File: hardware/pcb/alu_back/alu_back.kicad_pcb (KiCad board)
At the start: 2 copper layers, 132.1 x 114.3 mm, 31 parts, among them J1 SYNC, J2 BUS, J3 FLAGS, J4 OUT, J5 FCTL, J6 LOAD, J7 ARGS, J8 POWER, U1 Register A, U10 74HC125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

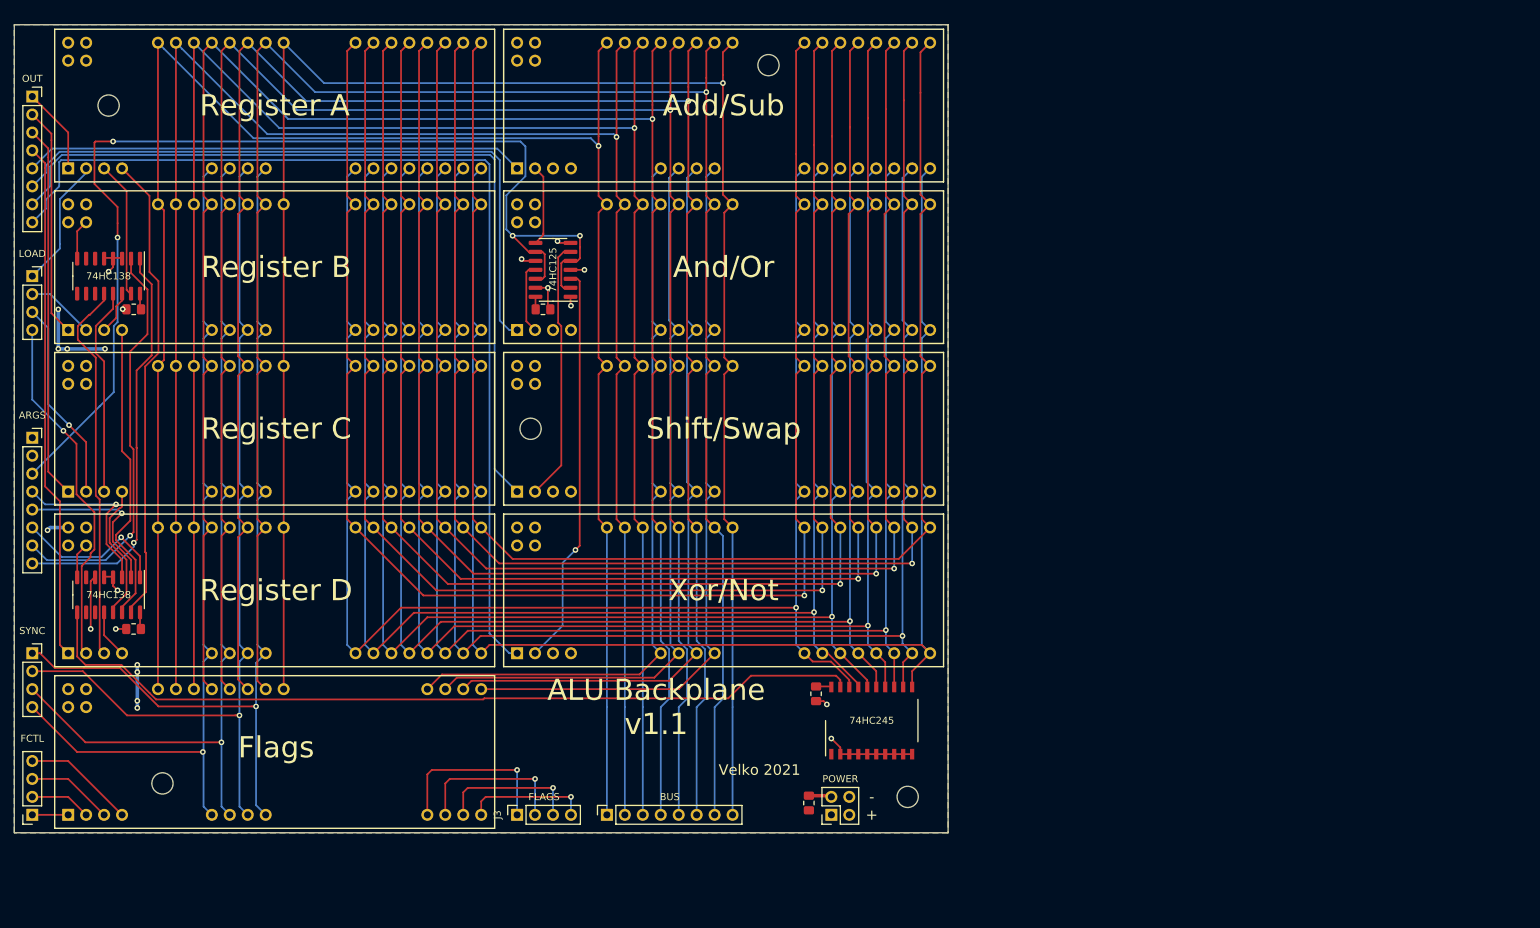
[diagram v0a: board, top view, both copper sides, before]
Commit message: Rewired with internal demuxes, cleaned board
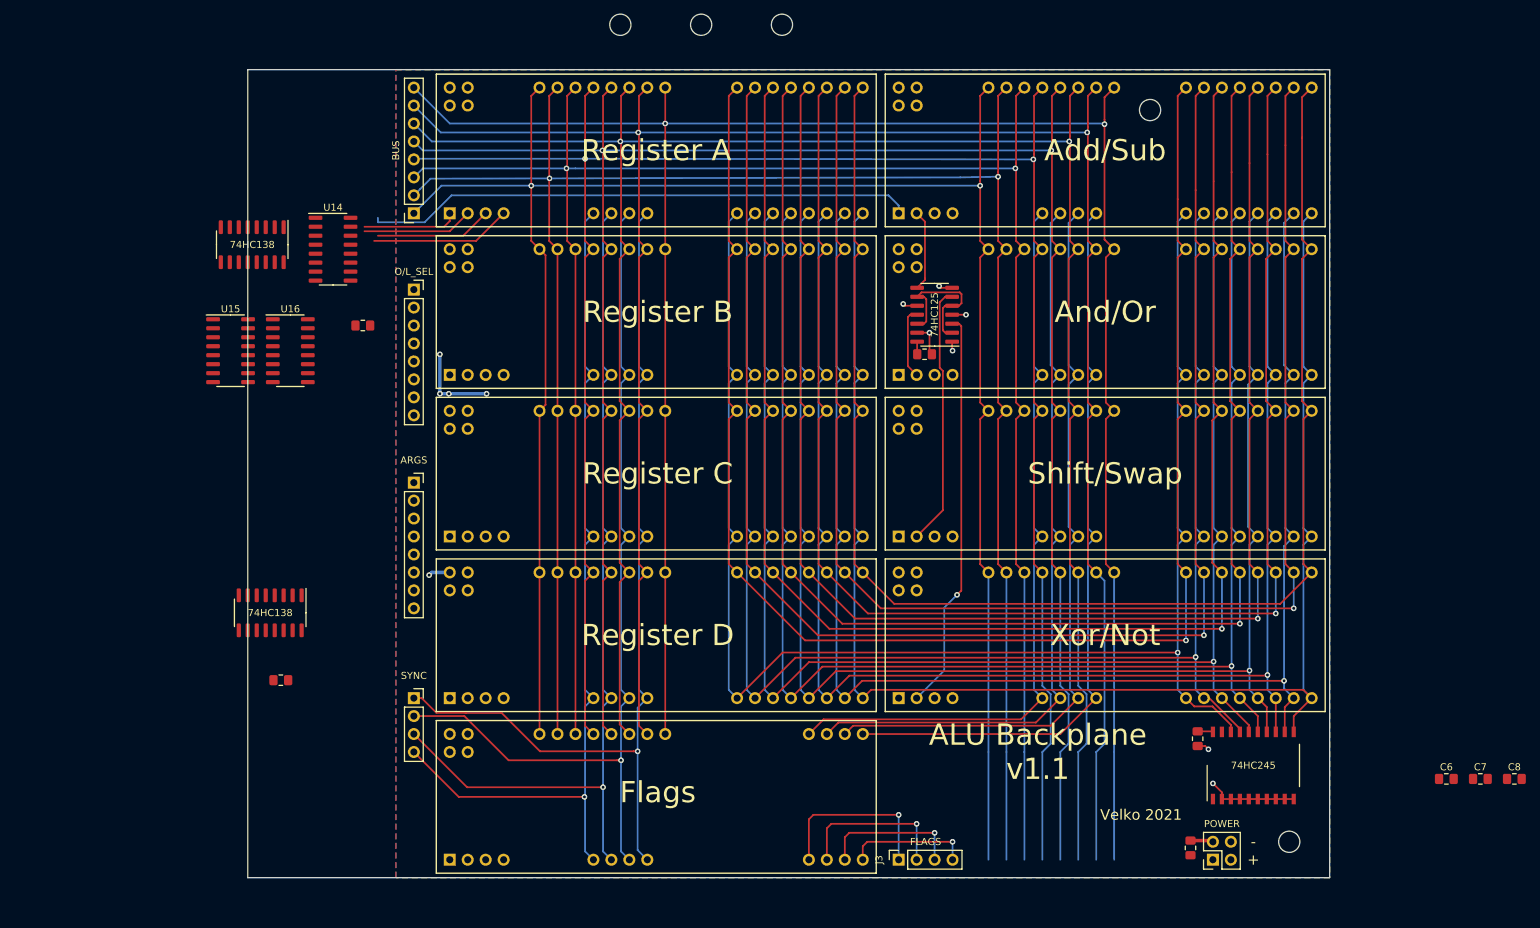
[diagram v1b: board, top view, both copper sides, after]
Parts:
- removed J5: FCTL, Connector_PinSocket_2.54mm:PinSocket_1x04_P2.54mm_Vertical
- removed J6: LOAD, Connector_PinSocket_2.54mm:PinSocket_1x04_P2.54mm_Vertical
- added C6: 100nF, Capacitor_SMD:C_0805_2012Metric_Pad1.18x1.45mm_HandSolder, F.Cu at (224.8, 131.4)
- added C7: 100nF, Capacitor_SMD:C_0805_2012Metric_Pad1.18x1.45mm_HandSolder, F.Cu at (229.6, 131.4)
- added C8: 100nF, Capacitor_SMD:C_0805_2012Metric_Pad1.18x1.45mm_HandSolder, F.Cu at (234.4, 131.4)
- added U14: 74HC138, Package_SO:SOIC-16_3.9x9.9mm_P1.27mm, F.Cu at (67.3, 56.5)
- added U15: 74HC138, Package_SO:SOIC-16_3.9x9.9mm_P1.27mm, F.Cu at (52.8, 70.9)
- added U16: 74HC138, Package_SO:SOIC-16_3.9x9.9mm_P1.27mm, F.Cu at (61.3, 70.9)
- J4: value OUT -> O/L_SEL
- moved H2 138.5 mm to (130.8, 24.8)
- moved J2 89.4 mm to (78.7, 51.4), turned to 180 degrees
- moved H1 73.3 mm to (108.0, 24.8)
- moved H5 62.0 mm to (119.4, 24.8)
- moved J4 60.5 mm to (78.7, 62.2)
- moved J8 54.3 mm to (191.8, 142.9)
- moved U11 54.3 mm to (197.5, 129.5)
- moved C4 54.3 mm to (151.0, 71.4)
- moved U1 54.3 mm to (81.9, 31.8)
- moved U10 54.3 mm to (152.4, 65.8)
- moved U2 54.3 mm to (81.9, 54.6)
- moved U3 54.3 mm to (81.9, 77.5)
- moved U4 54.3 mm to (81.9, 100.3)
- moved U9 54.3 mm to (81.9, 123.2)
- moved C1 54.3 mm to (188.6, 141.2)
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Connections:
- J4 pad 1: OUT_A -> OUT_SEL0
- J4 pad 2: OUT_B -> OUT_SEL1
- J4 pad 3: OUT_C -> OUT_SEL2
- J4 pad 4: OUT_D -> OUT_SEL3
- J4 pad 5: OUT_AS -> LOAD_SEL0
- J4 pad 6: OUT_AO -> LOAD_SEL1
- J4 pad 7: OUT_S -> LOAD_SEL2
- J4 pad 8: OUT_XN -> LOAD_SEL3
- J7 pad 1: (no net) -> CARRY
- J7 pad 2: (no net) -> F_CALC
- U9 pad 1: Net-(J5-Pad1) -> OUT_F
- U9 pad 2: Net-(J5-Pad2) -> LOAD_F
- U9 pad 3: Net-(J5-Pad3) -> F_CALC
- U9 pad 4: Net-(J5-Pad4) -> CARRY
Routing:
- net OUT_XN: track 142.7 -> 0.00 mm
- net ALT: track 159.1 -> 21.5 mm, vias 4 -> 0
- net ARG_ZR: track 119.3 -> 0.00 mm
- net OUT_S: track 118.5 -> 0.00 mm
- net OUT_AO: track 94.9 -> 0.00 mm
- net OUT_D: track 73.2 -> 0.00 mm
- net ARG_L0: track 57.9 -> 0.00 mm, vias 1 -> 0
- net ARG_L1: track 57.7 -> 0.00 mm, vias 1 -> 0
- net ARG_DL: track 53.9 -> 0.00 mm
- net OUT_C: track 52.9 -> 0.00 mm
- net LOAD_D: track 50.4 -> 0.00 mm, vias 1 -> 0
- net ARG_AR: track 66.7 -> 19.9 mm
- net ARG_BR: track 43.3 -> 0.00 mm
- net /BUS0: track 268.2 -> 303.5 mm, vias 1 -> 2
- net OUT_B: track 32.6 -> 0.00 mm
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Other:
- board size 132.1 x 114.3 mm -> 153 x 114.3 mm

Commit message: Rewired busses on front vertically, back horizontally
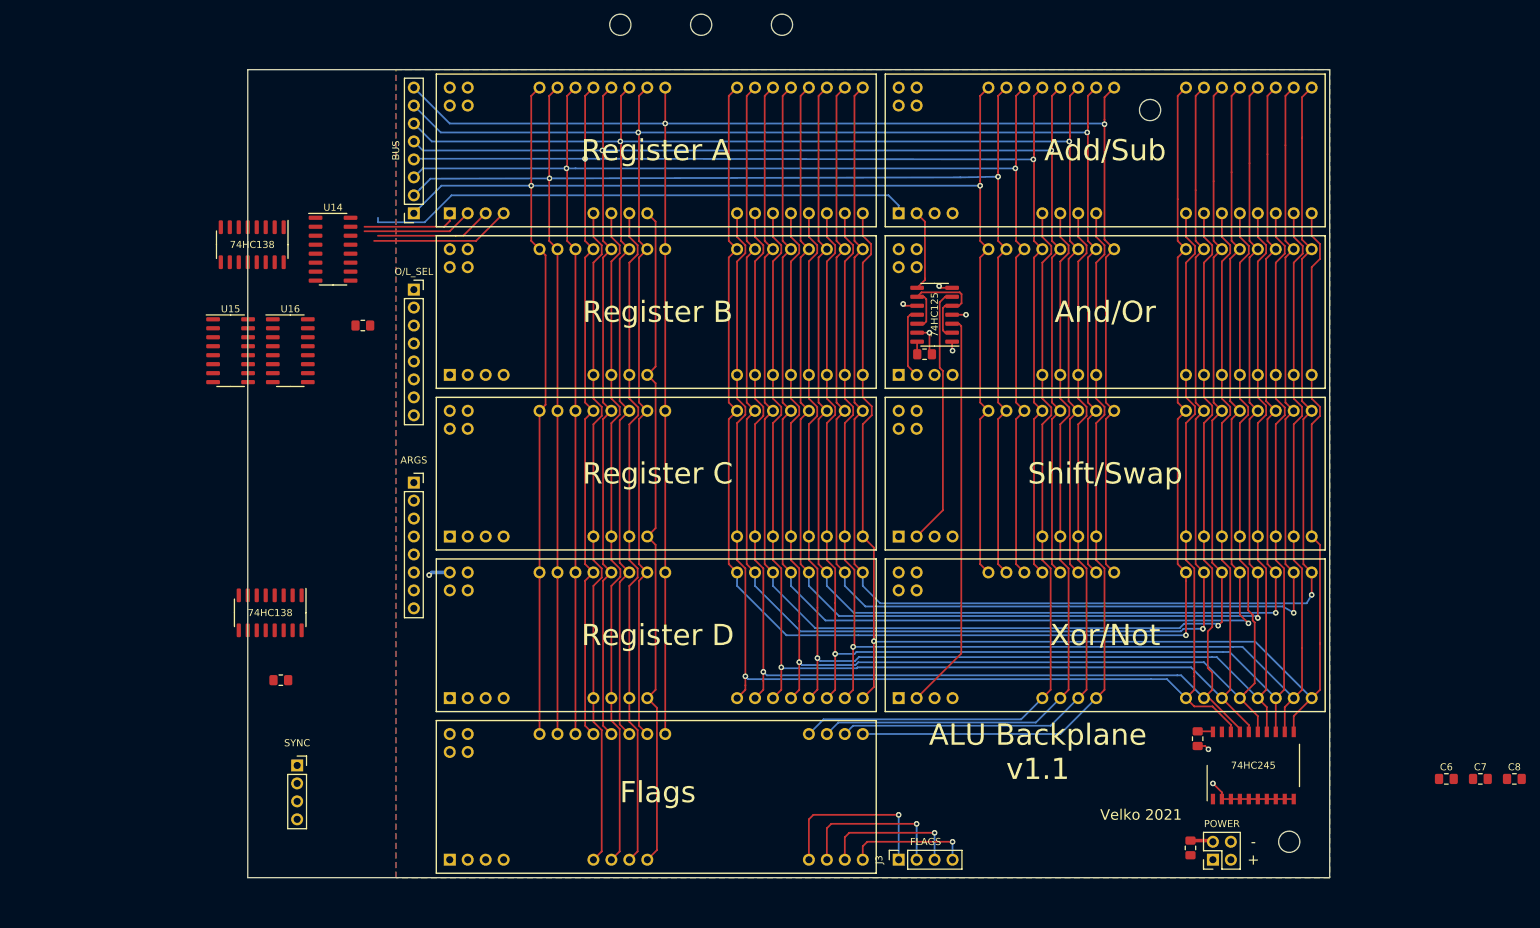
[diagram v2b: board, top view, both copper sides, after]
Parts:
- moved J1 19.1 mm to (62.2, 129.5)
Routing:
- net /BUS2: track 302.8 -> 261.2 mm
- net /BUS1: track 305.3 -> 263.7 mm
- net /BUS4: track 296.1 -> 254.5 mm
- net /BUS3: track 299.1 -> 257.5 mm
- net /BUS0: track 303.5 -> 262.9 mm
- net /BUS7: track 287.0 -> 246.3 mm
- net /BUS6: track 288.2 -> 247.5 mm
- net /BUS5: track 290.2 -> 249.5 mm
- net ~RESET~: track 130.3 -> 95.5 mm, vias 1 -> 0
- net RESET: track 127.2 -> 95.4 mm, vias 1 -> 0
- net ~CLK~: track 125.2 -> 95.4 mm, vias 1 -> 0
- net CLK: track 122.1 -> 95.3 mm, vias 1 -> 0
- net VCC: track 22.0 -> 7.06 mm, vias 5 -> 1
- net /L0: track 210.5 -> 213.6 mm, vias 0 -> 1
- net /L4: track 216.9 -> 219.7 mm
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
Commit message: Re-routed ALU backplane
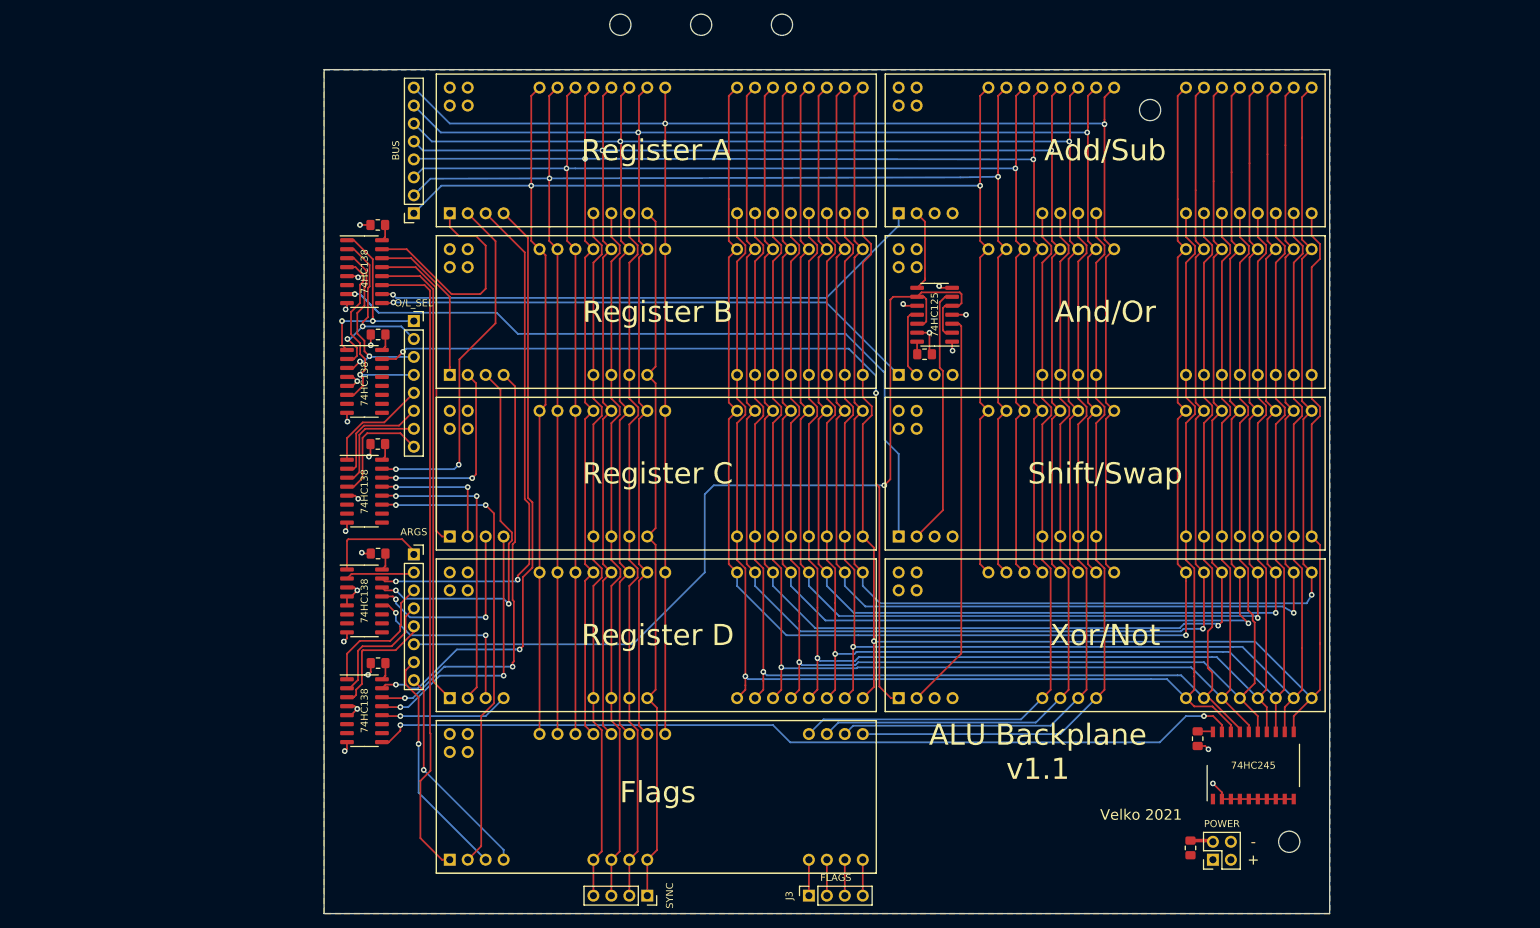
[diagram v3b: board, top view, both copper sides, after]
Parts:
- moved C8 161.6 mm to (73.7, 115.1), turned to 180 degrees
- moved C7 159.1 mm to (73.7, 99.6), turned to 180 degrees
- moved C6 158.4 mm to (73.6, 84.1), turned to 180 degrees
- moved U13 67.8 mm to (71.8, 121.8), turned to 0 degrees
- moved J1 52.8 mm to (111.8, 148.0), turned to 270 degrees
- moved C2 50.8 mm to (73.7, 68.6)
- moved U15 27.4 mm to (71.8, 90.7)
- moved C3 14.4 mm to (73.6, 53.1)
- moved J3 13.7 mm to (134.6, 148.0)
- moved U12 13.4 mm to (71.8, 106.3), turned to 0 degrees
- moved U16 11.4 mm to (71.8, 75.2)
- moved J7 10.2 mm to (78.7, 99.7)
- moved U14 5.46 mm to (71.8, 59.7)
- moved J4 4.45 mm to (78.7, 66.7)
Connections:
- J7 pad 1: CARRY -> ARG_L0
- J7 pad 2: F_CALC -> ARG_L1
- J7 pad 3: ALT -> ARG_R0
- J7 pad 4: ARG_R2 -> ARG_R1
- J7 pad 5: ARG_R1 -> ARG_R2
- J7 pad 6: ARG_R0 -> ALT
- J7 pad 7: ARG_L1 -> F_CALC
- J7 pad 8: ARG_L0 -> CARRY
- U12 pad 1: ARG_R0 -> ARG_L0
- U12 pad 12: ARG_DR -> ARG_DL
- U12 pad 13: ARG_CR -> ARG_CL
- U12 pad 14: ARG_BR -> ARG_BL
- U12 pad 15: ARG_AR -> ARG_AL
- U12 pad 2: ARG_R1 -> ARG_L1
- U12 pad 3: ARG_R2 -> GND
- U12 pad 9: ARG_ZR -> (no net)
- U13 pad 1: ARG_L0 -> ARG_R0
- U13 pad 12: ARG_DL -> ARG_DR
- U13 pad 13: ARG_CL -> ARG_CR
- U13 pad 14: ARG_BL -> ARG_BR
- U13 pad 15: ARG_AL -> ARG_AR
- U13 pad 2: ARG_L1 -> ARG_R1
- U13 pad 3: GND -> ARG_R2
- U13 pad 9: (no net) -> ARG_ZR
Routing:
- net ARG_ZR: track 0.00 -> 124.3 mm, vias 0 -> 2
- net OUT_XN: track 0.00 -> 119.6 mm, vias 0 -> 2
- net ALT: track 21.5 -> 134.4 mm, vias 0 -> 1
- net OUT_S: track 0.00 -> 108.9 mm, vias 0 -> 1
- net OUT_F: track 0.00 -> 90.6 mm
- net OUT_AO: track 0.00 -> 77.4 mm, vias 0 -> 1
- net LOAD_F: track 0.00 -> 66.9 mm, vias 0 -> 2
- net OUT_D: track 0.00 -> 66.8 mm
- net ARG_AR: track 19.9 -> 86.3 mm, vias 0 -> 2
- net ARG_BR: track 0.00 -> 62.8 mm, vias 0 -> 2
- net ARG_AL: track 16.6 -> 74.5 mm, vias 0 -> 2
- net ARG_BL: track 0.00 -> 53.0 mm, vias 0 -> 2
- net OUT_C: track 0.00 -> 45.5 mm
- net LOAD_D: track 0.00 -> 42.5 mm, vias 0 -> 2
- net ARG_CR: track 0.00 -> 38.8 mm, vias 0 -> 2
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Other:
- board size 153 x 114.3 mm -> 142.2 x 119.4 mm
